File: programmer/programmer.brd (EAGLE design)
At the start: 13.7 x 15 mm, 5 parts

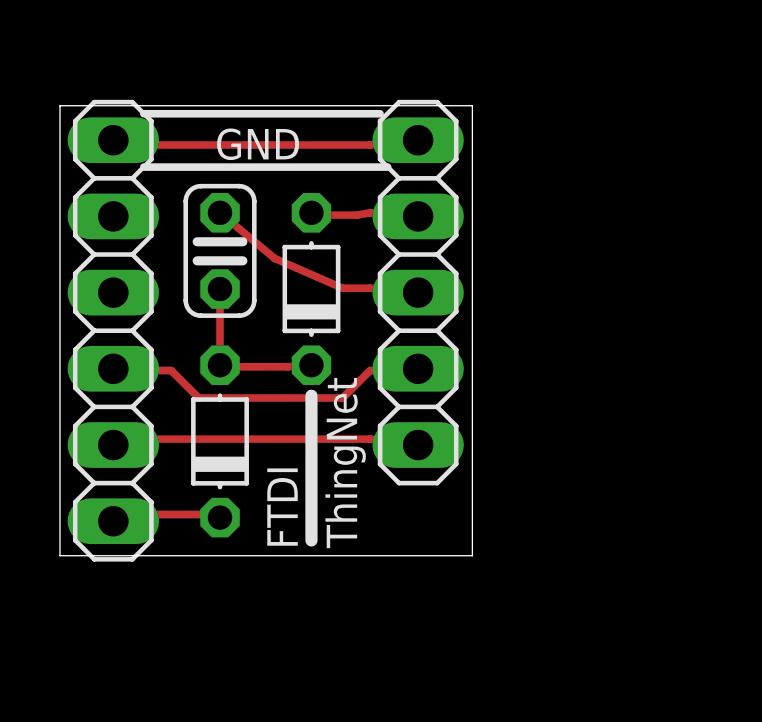
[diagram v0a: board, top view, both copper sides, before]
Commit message: Updated programmer board and organized everything into folders
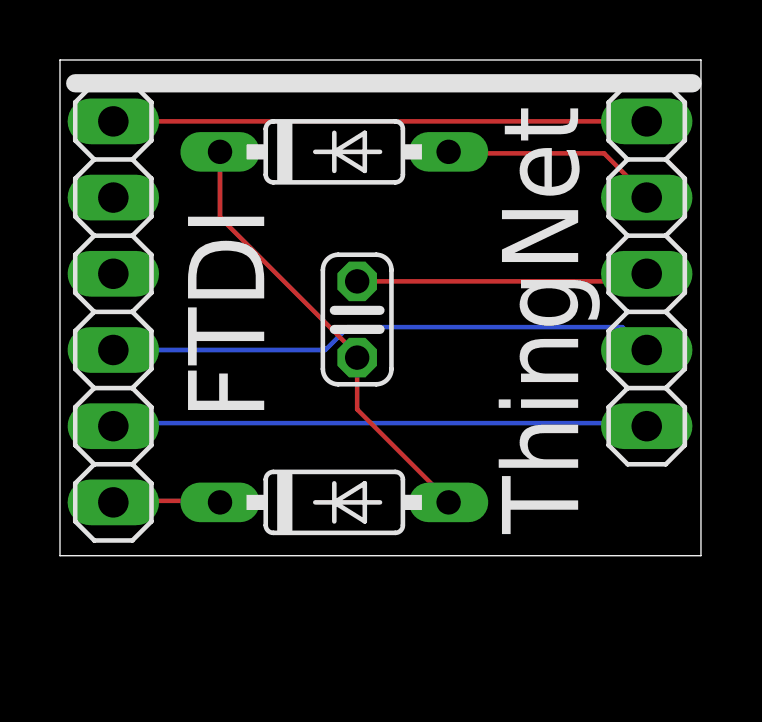
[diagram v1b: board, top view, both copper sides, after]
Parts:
- D1, D2: device diode:D-5 -> diode:DO35-7
- moved THINGNET 7.65 mm to (19.6, 9.40)
- moved C1 5.11 mm to (9.91, 7.87)
- moved D2 4.64 mm to (9.14, 13.5), turned to 0 degrees
- moved D1 4.32 mm to (9.14, 1.78), turned to 0 degrees
- moved FTDI 0.63 mm to (1.78, 8.13)
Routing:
- net N$1: track 6.10 -> 14.8 mm
- net TXD: track 10.2 -> 17.9 mm
- net GND: track 10.2 -> 17.8 mm
- net RXD: track 10.9 -> 18.4 mm
- net GPIO0: track 4.19 -> 7.29 mm
- net CH_PD: track 7.37 -> 9.78 mm
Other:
- board size 13.7 x 15 mm -> 21.4 x 16.5 mm
- board text removed: "GND"
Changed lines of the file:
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@@
 <setting verticaltext="up"/>
 </settings>
-<grid distance="0.01" unitdist="inch" unit="mm" style="lines" multiple="1" display="no" altdistance="0.025" altunitdist="inch" altunit="inch"/>
+<grid distance="0.01" unitdist="inch" unit="inch" style="lines" multiple="1" display="no" altdistance="0.025" altunitdist="inch" altunit="inch"/>
 <layers>
 <layer number="1" name="Top" color="4" fill="1" visible="yes" active="yes"/>
@@
 <board>
 <plain>
-<wire x1="0" y1="0" x2="13.746" y2="0" width="0" layer="20"/>
-<wire x1="13.746" y1="0" x2="13.746" y2="15" width="0" layer="20"/>
-<wire x1="13.746" y1="15" x2="0" y2="15" width="0" layer="20"/>
-<wire x1="0" y1="15" x2="0" y2="0" width="0" layer="20"/>
-<text x="6.604" y="13.716" size="1.016" layer="25" align="center">GND</text>
-<wire x1="2.794" y1="12.954" x2="10.922" y2="12.954" width="0.254" layer="25"/>
-<wire x1="8.382" y1="0.508" x2="8.382" y2="5.334" width="0.4064" layer="25"/>
-<wire x1="2.794" y1="14.732" x2="10.668" y2="14.732" width="0.254" layer="25"/>
-<text x="9.906" y="0.254" size="1.016" layer="25" rot="R90">ThingNet</text>
+<wire x1="0" y1="0" x2="21.366" y2="0" width="0" layer="20"/>
+<wire x1="21.366" y1="0" x2="21.366" y2="16.524" width="0" layer="20"/>
+<wire x1="21.366" y1="16.524" x2="0" y2="16.524" width="0" layer="20"/>
+<wire x1="0" y1="16.524" x2="0" y2="0" width="0" layer="20"/>
+<wire x1="0.508" y1="15.748" x2="21.082" y2="15.748" width="0.6096" layer="25"/>
+<text x="14.732" y="14.986" size="2.54" layer="25" rot="R270">ThingNet</text>
 </plain>
 <attributes>
@@
 <param name="PrefDir.14" value="0"/>
 <param name="PrefDir.15" value="0"/>
-<param name="PrefDir.16" value="0"/>
+<param name="PrefDir.16" value="a"/>
 <param name="cfVia" value="8"/>
 <param name="cfNonPref" value="5"/>
@@
 </autorouter>
 <elements>
-<element name="C1" library="rcl" package="C025-024X044" value="100nF" x="5.334" y="10.16" smashed="yes" rot="R270"/>
-<element name="D1" library="diode" package="D-5" value="B5819W" x="5.334" y="3.81" smashed="yes" rot="R90"/>
-<element name="D2" library="diode" package="D-5" value="Schottky Barrier low Vf (0.6v)" x="8.382" y="8.89" smashed="yes" rot="R90"/>
-<element name="FTDI" library="pinhead" package="1X06" value="" x="1.778" y="7.5" smashed="yes" rot="R90">
-<attribute name="NAME" x="7.9248" y="0.2102" size="1.016" layer="25" ratio="10" rot="R90"/>
-<attribute name="VALUE" x="4.953" y="-0.12" size="1.27" layer="27" rot="R90"/>
+<element name="C1" library="rcl" package="C025-024X044" value="100nF" x="9.906" y="7.874" smashed="yes" rot="R270"/>
+<element name="D1" library="diode" package="DO35-7" value="B5819W" x="9.144" y="1.778" smashed="yes"/>
+<element name="D2" library="diode" package="DO35-7" value="Schottky Barrier low Vf (0.6v)" x="9.144" y="13.462" smashed="yes"/>
+<element name="FTDI" library="pinhead" package="1X06" value="" x="1.778" y="8.128" smashed="yes" rot="R90">
+<attribute name="NAME" x="4.2672" y="11.6078" size="2.54" layer="25" ratio="10" rot="R270"/>
+<attribute name="VALUE" x="4.953" y="0.508" size="1.27" layer="27" rot="R90"/>
 </element>
-<element name="THINGNET" library="pinhead" package="1X05" value="" x="11.938" y="8.77" smashed="yes" rot="R90">
-<attribute name="VALUE" x="15.113" y="2.42" size="1.27" layer="27" rot="R90"/>
+<element name="THINGNET" library="pinhead" package="1X05" value="" x="19.558" y="9.398" smashed="yes" rot="R90">
+<attribute name="VALUE" x="22.733" y="3.048" size="1.27" layer="27" rot="R90"/>
 </element>
 </elements>
@@
 <contactref element="THINGNET" pad="5"/>
 <contactref element="FTDI" pad="6"/>
-<wire x1="10.3378" y1="13.6906" x2="2.1082" y2="13.6906" width="0.254" layer="1"/>
-<wire x1="2.1082" y1="13.6906" x2="1.778" y2="13.85" width="0.254" layer="1"/>
-<wire x1="10.3378" y1="13.6906" x2="11.938" y2="13.85" width="0.254" layer="1"/>
+<wire x1="19.558" y1="14.478" x2="1.778" y2="14.478" width="0.1524" layer="1"/>
 </signal>
 <signal name="TXD">
 <contactref element="THINGNET" pad="1"/>
 <contactref element="FTDI" pad="2"/>
-<wire x1="10.3378" y1="3.8862" x2="2.1082" y2="3.8862" width="0.254" layer="1"/>
-<wire x1="2.1082" y1="3.8862" x2="1.778" y2="3.69" width="0.254" layer="1"/>
-<wire x1="10.3378" y1="3.8862" x2="11.938" y2="3.69" width="0.254" layer="1"/>
+<wire x1="19.5072" y1="4.4196" x2="1.8288" y2="4.4196" width="0.1524" layer="16"/>
+<wire x1="1.8288" y1="4.4196" x2="1.778" y2="4.318" width="0.1524" layer="16"/>
+<wire x1="19.5072" y1="4.4196" x2="19.558" y2="4.318" width="0.1524" layer="16"/>
 </signal>
 <signal name="RXD">
 <contactref element="THINGNET" pad="2"/>
 <contactref element="FTDI" pad="3"/>
-<wire x1="3.7084" y1="6.1722" x2="2.1082" y2="6.1722" width="0.254" layer="1"/>
-<wire x1="4.6228" y1="5.2578" x2="3.7084" y2="6.1722" width="0.254" layer="1"/>
-<wire x1="9.4234" y1="5.2578" x2="4.6228" y2="5.2578" width="0.254" layer="1"/>
-<wire x1="10.3378" y1="6.1722" x2="9.4234" y2="5.2578" width="0.254" layer="1"/>
-<wire x1="2.1082" y1="6.1722" x2="1.778" y2="6.23" width="0.254" layer="1"/>
-<wire x1="10.3378" y1="6.1722" x2="11.938" y2="6.23" width="0.254" layer="1"/>
+<wire x1="8.8392" y1="6.858" x2="1.778" y2="6.858" width="0.1524" layer="16"/>
+<wire x1="9.6012" y1="7.62" x2="8.8392" y2="6.858" width="0.1524" layer="16"/>
+<wire x1="18.7452" y1="7.62" x2="9.6012" y2="7.62" width="0.1524" layer="16"/>
+<wire x1="19.5072" y1="6.858" x2="18.7452" y2="7.62" width="0.1524" layer="16"/>
+<wire x1="19.5072" y1="6.858" x2="19.558" y2="6.858" width="0.1524" layer="16"/>
 </signal>
 <signal name="GPIO0">
 <contactref element="THINGNET" pad="4"/>
 <contactref element="D2" pad="A"/>
-<wire x1="9.906" y1="11.3538" x2="8.0772" y2="11.3538" width="0.254" layer="1"/>
-<wire x1="10.3378" y1="11.43" x2="9.906" y2="11.3538" width="0.254" layer="1"/>
-<wire x1="8.0772" y1="11.3538" x2="8.382" y2="11.43" width="0.254" layer="1"/>
-<wire x1="10.3378" y1="11.43" x2="11.938" y2="11.31" width="0.254" layer="1"/>
+<wire x1="18.1356" y1="13.4112" x2="12.954" y2="13.4112" width="0.1524" layer="1"/>
+<wire x1="19.5072" y1="12.0396" x2="18.1356" y2="13.4112" width="0.1524" layer="1"/>
+<wire x1="12.954" y1="13.4112" x2="12.954" y2="13.462" width="0.1524" layer="1"/>
+<wire x1="19.5072" y1="12.0396" x2="19.558" y2="11.938" width="0.1524" layer="1"/>
 </signal>
 <signal name="CH_PD">
 <contactref element="THINGNET" pad="3"/>
 <contactref element="C1" pad="1"/>
-<wire x1="7.1628" y1="9.906" x2="5.334" y2="11.43" width="0.254" layer="1"/>
-<wire x1="9.4234" y1="8.9154" x2="7.1628" y2="9.906" width="0.254" layer="1"/>
-<wire x1="10.3378" y1="8.9154" x2="9.4234" y2="8.9154" width="0.254" layer="1"/>
-<wire x1="10.3378" y1="8.9154" x2="11.938" y2="8.77" width="0.254" layer="1"/>
+<wire x1="19.3548" y1="9.144" x2="9.906" y2="9.144" width="0.1524" layer="1"/>
+<wire x1="19.5072" y1="9.2964" x2="19.3548" y2="9.144" width="0.1524" layer="1"/>
+<wire x1="19.5072" y1="9.2964" x2="19.558" y2="9.398" width="0.1524" layer="1"/>
 </signal>
 <signal name="DTR">
 <contactref element="D1" pad="C"/>
 <contactref element="FTDI" pad="1"/>
-<wire x1="2.1082" y1="1.3716" x2="5.08" y2="1.3716" width="0.254" layer="1"/>
-<wire x1="5.08" y1="1.3716" x2="5.334" y2="1.27" width="0.254" layer="1"/>
-<wire x1="2.1082" y1="1.3716" x2="1.778" y2="1.15" width="0.254" layer="1"/>
+<wire x1="1.8288" y1="1.8288" x2="5.334" y2="1.8288" width="0.1524" layer="1"/>
+<wire x1="5.334" y1="1.8288" x2="5.334" y2="1.778" width="0.1524" layer="1"/>
+<wire x1="1.8288" y1="1.8288" x2="1.778" y2="1.778" width="0.1524" layer="1"/>
 </signal>
 <signal name="N$1">
@@
 <contactref element="D2" pad="C"/>
 <contactref element="D1" pad="A"/>
-<wire x1="5.334" y1="8.89" x2="5.334" y2="6.35" width="0.254" layer="1"/>
-<wire x1="5.08" y1="6.2992" x2="5.334" y2="6.35" width="0.254" layer="1"/>
-<wire x1="5.08" y1="6.2992" x2="7.5946" y2="6.2992" width="0.254" layer="1"/>
-<wire x1="7.5946" y1="6.2992" x2="8.382" y2="6.35" width="0.254" layer="1"/>
+<wire x1="9.906" y1="4.8768" x2="9.906" y2="6.604" width="0.1524" layer="1"/>
+<wire x1="12.954" y1="1.8288" x2="9.906" y2="4.8768" width="0.1524" layer="1"/>
+<wire x1="12.954" y1="1.8288" x2="12.954" y2="1.778" width="0.1524" layer="1"/>
+<wire x1="5.334" y1="11.2776" x2="5.334" y2="13.462" width="0.1524" layer="1"/>
+<wire x1="9.906" y1="6.7056" x2="5.334" y2="11.2776" width="0.1524" layer="1"/>
+<wire x1="9.906" y1="6.7056" x2="9.906" y2="6.604" width="0.1524" layer="1"/>
 </signal>
 <signal name="VCC">
